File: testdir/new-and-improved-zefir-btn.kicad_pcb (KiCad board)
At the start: 2 copper layers, 44 x 43.6 mm, 56 parts, among them J1 USB_C_Receptacle_USB2.0_16P, J2 Conn_01x03_Socket, SW1 SW_Push_Dual, U1 BQ24074RGT, U2 ESP32-C3, U3 W25Q32JVZP, U4 USBLC6-2P6, U6 XC6206PxxxMR, Y1 40MHz

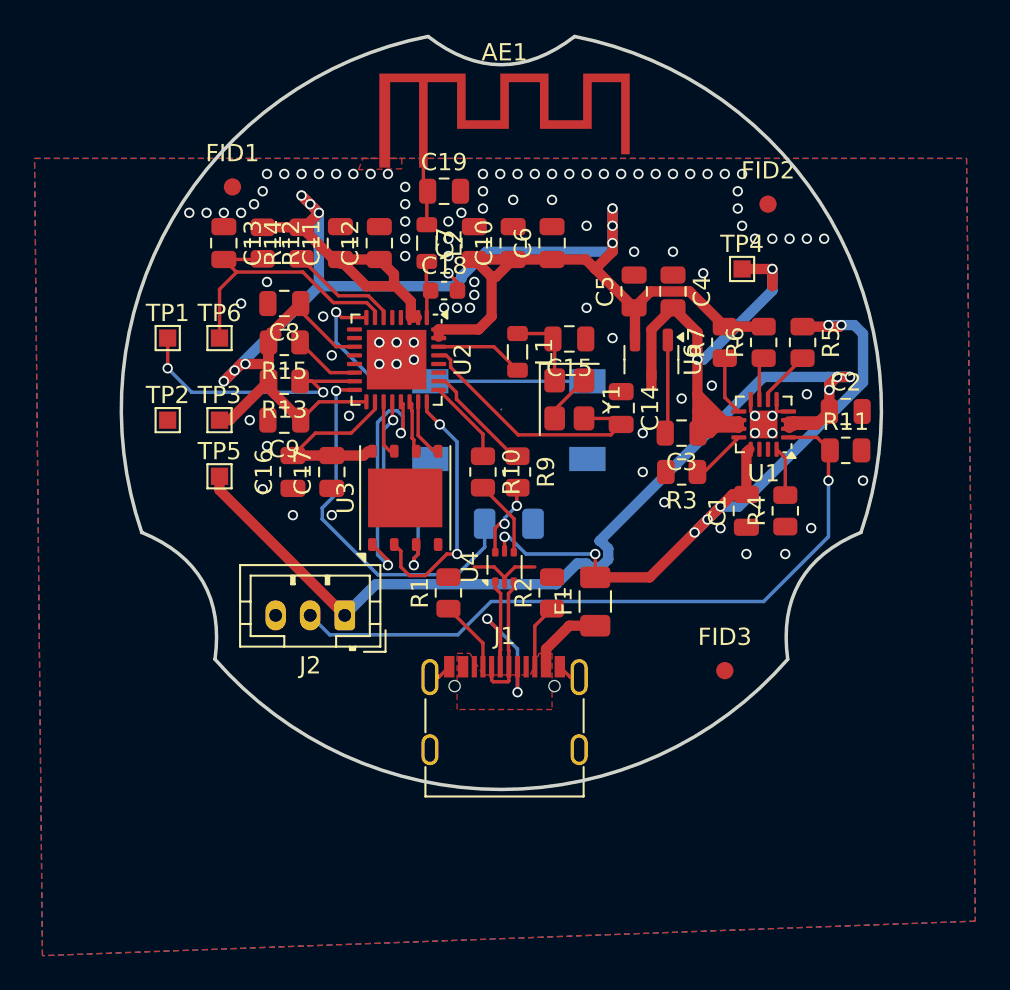
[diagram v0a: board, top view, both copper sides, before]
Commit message: no isolation yet, but close
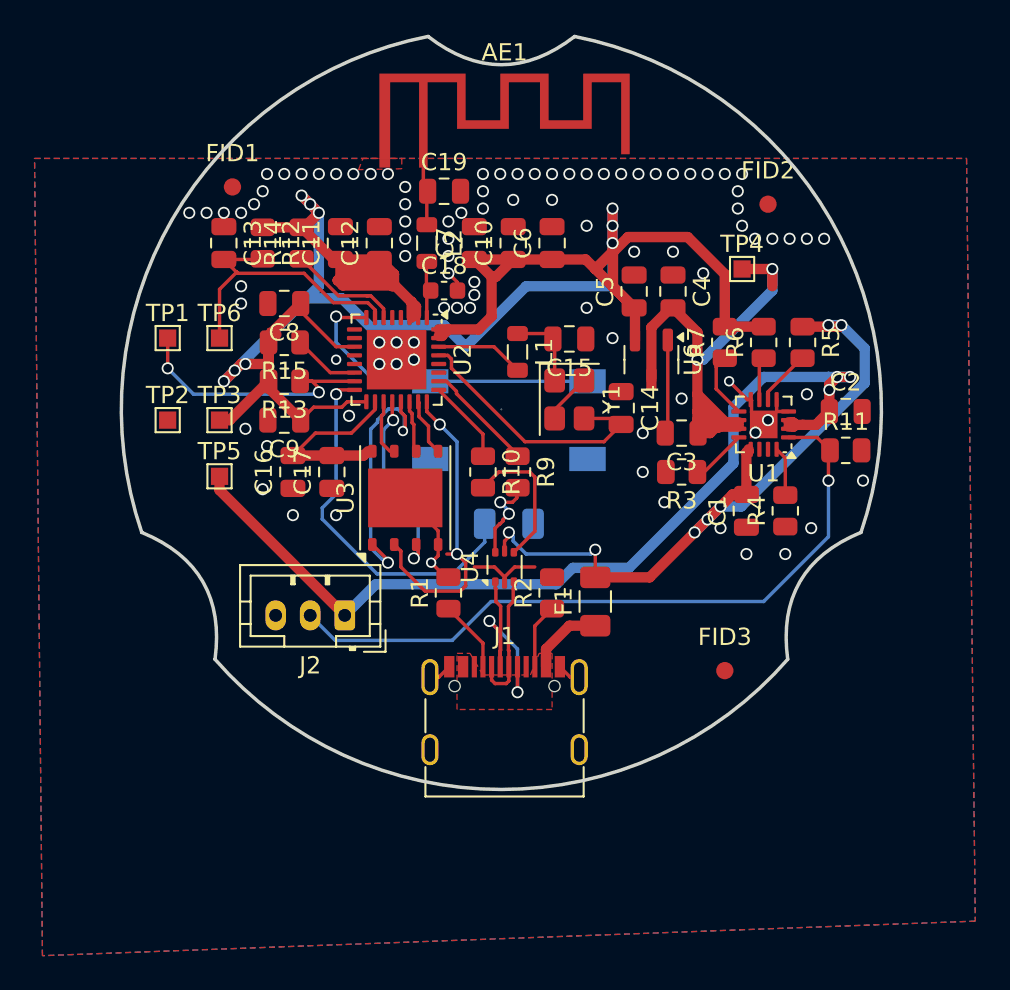
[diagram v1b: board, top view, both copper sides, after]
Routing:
- net +3V3: track 114.6 -> 139.6 mm
- net GND: track 19.4 -> 27.5 mm, vias 94 -> 92
- net /D_N: track 4.49 -> 8.36 mm
- net /FLASH_IO1: track 15.0 -> 18.1 mm
- net VBatt: track 57.5 -> 56.4 mm
- net /FLASH_IO2: track 12.0 -> 11.2 mm
- net /D_P: track 4.45 -> 5.12 mm
